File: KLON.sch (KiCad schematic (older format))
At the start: 69 parts, among them IC1 MAX1044ESA+, J1 Conn_01x03, J2 Conn_01x03, J3 Conn_01x02, SW1 3PDT, U1 TL072, U2 TL072

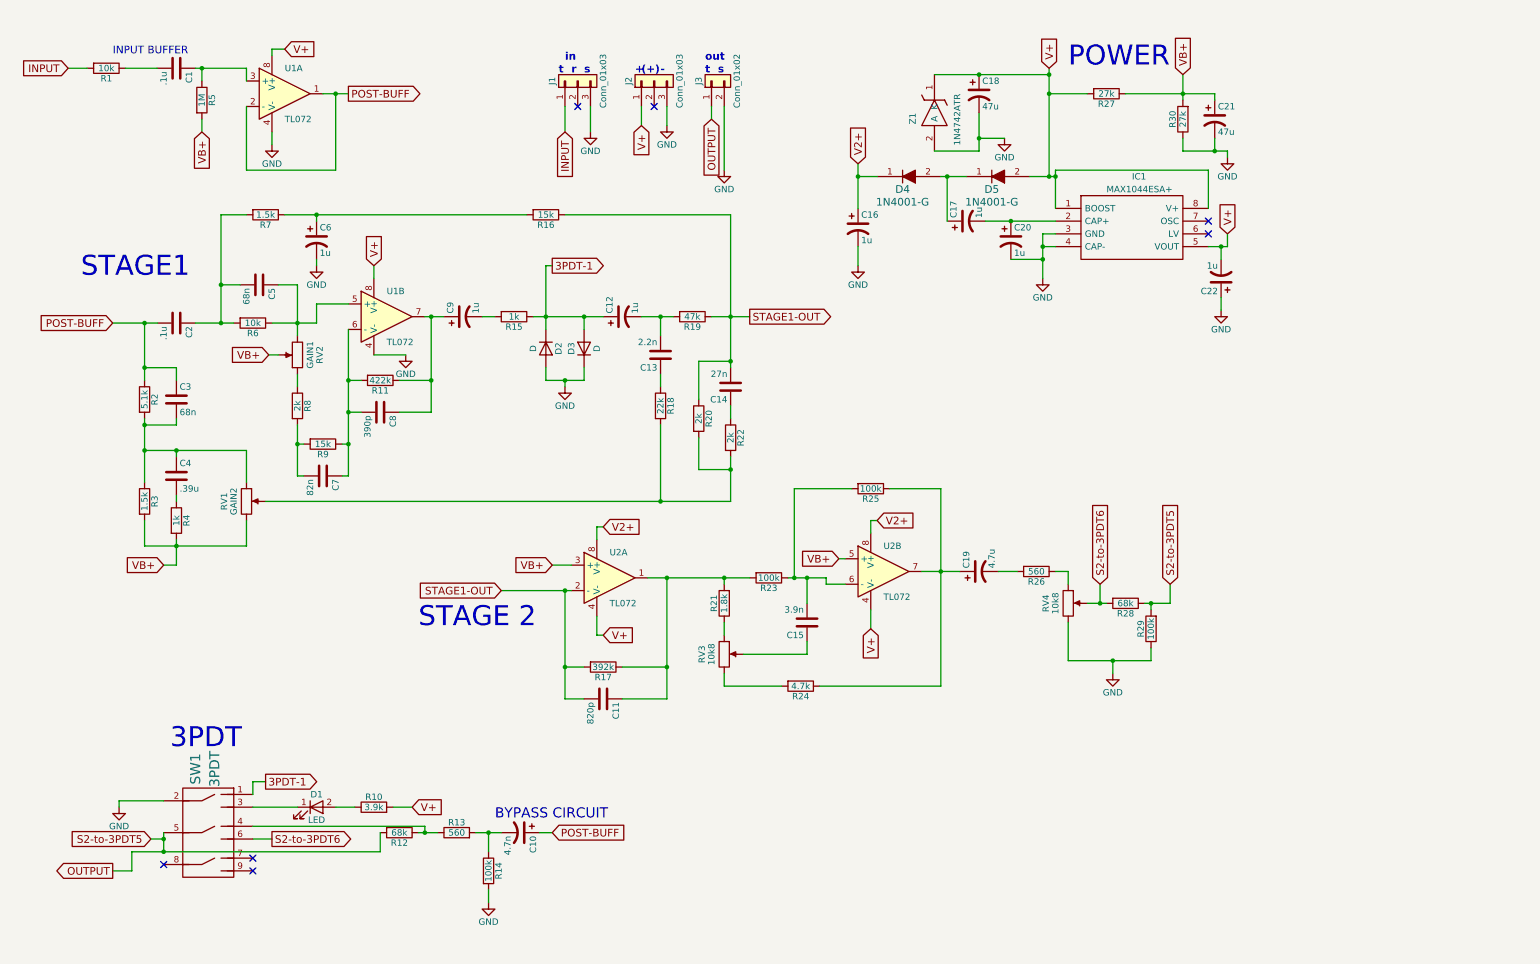
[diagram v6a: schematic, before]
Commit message: added Capacitor Footprints to CSV, added capacitors to digikey BOM (will put link or .xlsx file here later)
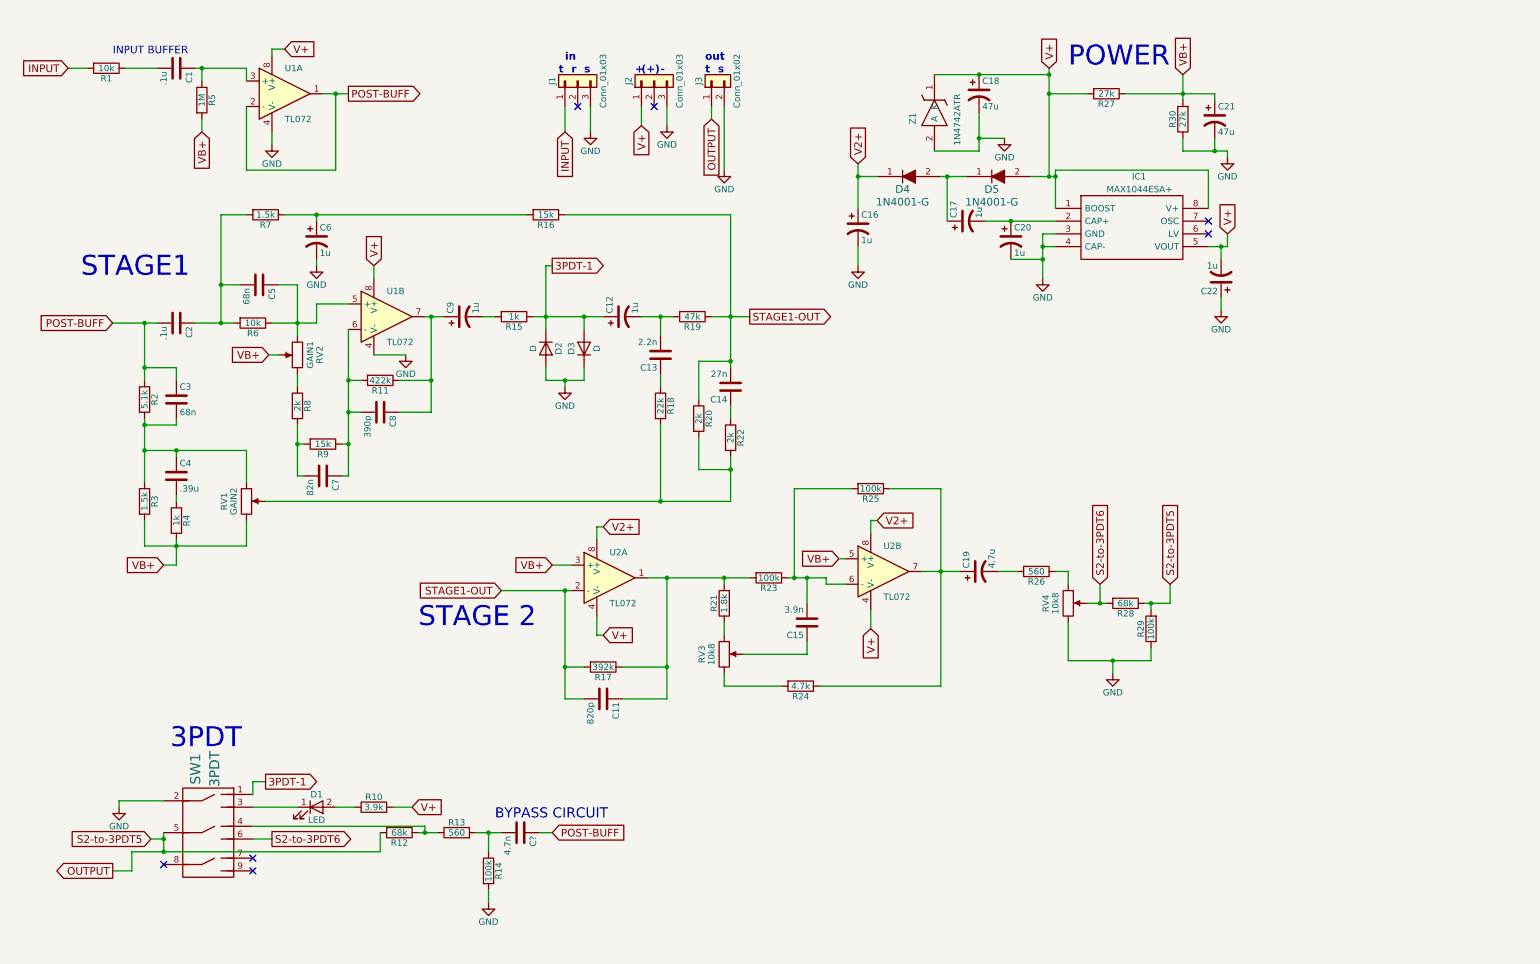
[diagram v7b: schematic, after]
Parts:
- removed C10: 4.7n, Capacitors_THT:C_Rect_L7.0mm_W2.0mm_P5.00mm, symbol CP1
- added C?: 4.7n, symbol C
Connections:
- net POST-BUFF: now also C?.1
- net at R13.2, R14.1: now also C?.2
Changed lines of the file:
@@
 	1300 700  1550 700
 Wire Wire Line
-	1850 700  2250 700
+	1850 700  1900 700
+Wire Wire Line
+	1900 700  2250 700
 Wire Wire Line
 	1900 700  1900 800
@@
 	2950 1500 2950 900
 Wire Wire Line
-	2850 900  3050 900
+	2850 900  2950 900
+Wire Wire Line
+	2950 900  3050 900
 Wire Wire Line
 	2550 550  2450 550
@@
 Connection ~ 2950 900
 Wire Wire Line
-	1850 2700 2150 2700
+	1850 2700 2050 2700
+Wire Wire Line
+	2050 2700 2150 2700
 Wire Wire Line
 	2200 2400 2050 2400
 Wire Wire Line
-	2050 1850 2050 2700
+	2050 1850 2050 2400
+Wire Wire Line
+	2050 2400 2050 2700
 Connection ~ 2050 2700
 Wire Wire Line
-	1200 2700 1550 2700
-Wire Wire Line
-	1450 2700 1450 3150
+	1200 2700 1450 2700
+Wire Wire Line
+	1450 2700 1550 2700
+Wire Wire Line
+	1450 2700 1450 3050
+Wire Wire Line
+	1450 3050 1450 3150
 Connection ~ 1450 2700
 Wire Wire Line
@@
 Connection ~ 2650 2700
 Wire Wire Line
-	2650 2400 2650 2800
+	2650 2400 2650 2700
+Wire Wire Line
+	2650 2700 2650 2800
 Wire Wire Line
 	3050 3900 3000 3900
@@
 	2650 3200 2650 3100
 Wire Wire Line
-	2650 3500 2650 3900
+	2650 3500 2650 3650
+Wire Wire Line
+	2650 3650 2650 3900
 Wire Wire Line
 	2650 3900 2700 3900
@@
 	3450 3150 3700 3150
 Wire Wire Line
-	2450 2700 2800 2700
-Wire Wire Line
-	3050 2750 3050 3900
+	2450 2700 2650 2700
+Wire Wire Line
+	2650 2700 2800 2700
+Wire Wire Line
+	3050 2750 3050 3150
+Wire Wire Line
+	3050 3150 3050 3400
+Wire Wire Line
+	3050 3400 3050 3650
+Wire Wire Line
+	3050 3650 3050 3900
 Wire Wire Line
 	2800 2700 2800 2550
@@
 	3500 2950 3250 2950
 Wire Wire Line
-	2550 1850 4450 1850
+	2550 1850 2800 1850
+Wire Wire Line
+	2800 1850 4450 1850
 Wire Wire Line
 	2800 1850 2800 1900
@@
 Connection ~ 2050 2400
 Wire Wire Line
-	3650 2650 3800 2650
-Wire Wire Line
-	3700 2650 3700 3400
+	3650 2650 3700 2650
+Wire Wire Line
+	3700 2650 3800 2650
+Wire Wire Line
+	3700 2650 3700 3150
+Wire Wire Line
+	3700 3150 3700 3400
 Connection ~ 3700 2650
 Connection ~ 3700 3150
@@
 	4600 3050 4600 3150
 Wire Wire Line
-	4600 3150 4900 3150
+	4600 3150 4750 3150
+Wire Wire Line
+	4750 3150 4900 3150
 Wire Wire Line
 	4900 3150 4900 3050
@@
 	3100 6500 2950 6500
 Wire Wire Line
-	4600 2250 4600 2750
+	4600 2250 4600 2650
+Wire Wire Line
+	4600 2650 4600 2750
 Connection ~ 4600 2650
 Wire Wire Line
@@
 Connection ~ 4900 2650
 Wire Wire Line
-	5350 2650 5600 2650
+	5350 2650 5500 2650
+Wire Wire Line
+	5500 2650 5600 2650
 Wire Wire Line
 	5500 3100 5500 3200
@@
 	1450 4250 1450 4450
 Wire Wire Line
-	1450 4450 2250 4450
+	1450 4450 1700 4450
+Wire Wire Line
+	1700 4450 2250 4450
 Wire Wire Line
 	2250 4450 2250 4250
 Connection ~ 1700 4450
 Wire Wire Line
-	1450 3700 2250 3700
+	1450 3700 1700 3700
+Wire Wire Line
+	1700 3700 2250 3700
 Connection ~ 1450 3700
 Wire Wire Line
@@
 	1700 4050 1700 4100
 Wire Wire Line
-	1700 4400 1700 4600
+	1700 4400 1700 4450
+Wire Wire Line
+	1700 4450 1700 4600
 Wire Wire Line
 	1700 4600 1600 4600
@@
 	4750 1850 6050 1850
 Wire Wire Line
-	6050 1850 6050 3050
-Wire Wire Line
-	5900 2650 6200 2650
-Wire Wire Line
-	6050 4100 2400 4100
-Wire Wire Line
-	6050 3750 6050 4100
-Wire Wire Line
-	1450 3450 1450 3950
-Wire Wire Line
-	4500 2650 5050 2650
+	6050 1850 6050 2650
+Wire Wire Line
+	6050 2650 6050 3000
+Wire Wire Line
+	6050 3000 6050 3050
+Wire Wire Line
+	5900 2650 6050 2650
+Wire Wire Line
+	6050 2650 6200 2650
+Wire Wire Line
+	6050 4100 5500 4100
+Wire Wire Line
+	5500 4100 2400 4100
+Wire Wire Line
+	6050 3750 6050 3850
+Wire Wire Line
+	6050 3850 6050 4100
+Wire Wire Line
+	1450 3450 1450 3500
+Wire Wire Line
+	1450 3500 1450 3700
+Wire Wire Line
+	1450 3700 1450 3950
+Wire Wire Line
+	4500 2650 4600 2650
+Wire Wire Line
+	4600 2650 4900 2650
+Wire Wire Line
+	4900 2650 5050 2650
 Wire Wire Line
 	5500 3500 5500 4100
@@
 Connection ~ 1450 3500
 Wire Wire Line
-	4250 4800 4800 4800
+	4250 4800 4750 4800
+Wire Wire Line
+	4750 4800 4800 4800
 Wire Wire Line
 	5050 4300 5000 4300
@@
 	4650 4600 4800 4600
 Wire Wire Line
-	4750 4800 4750 5650
+	4750 4800 4750 5400
+Wire Wire Line
+	4750 5400 4750 5650
 Wire Wire Line
 	4750 5400 4900 5400
@@
 Connection ~ 4750 5400
 Wire Wire Line
-	5400 4700 6200 4700
-Wire Wire Line
-	5550 4700 5550 5650
+	5400 4700 5550 4700
+Wire Wire Line
+	5550 4700 6000 4700
+Wire Wire Line
+	6000 4700 6200 4700
+Wire Wire Line
+	5550 4700 5550 5400
+Wire Wire Line
+	5550 5400 5550 5650
 Wire Wire Line
 	5550 5400 5200 5400
@@
 	6650 5300 6150 5300
 Wire Wire Line
-	6500 4700 6800 4700
+	6500 4700 6550 4700
+Wire Wire Line
+	6550 4700 6650 4700
+Wire Wire Line
+	6650 4700 6800 4700
 Wire Wire Line
 	6650 4700 6650 4900
 Wire Wire Line
-	7550 4650 7850 4650
-Wire Wire Line
-	7700 4000 7700 5550
+	7550 4650 7700 4650
+Wire Wire Line
+	7700 4650 7850 4650
+Wire Wire Line
+	7700 4000 7700 4650
+Wire Wire Line
+	7700 4650 7700 5550
 Wire Wire Line
 	7700 5550 6750 5550
@@
 	8700 5050 8700 5350
 Wire Wire Line
-	8700 5350 9350 5350
+	8700 5350 9050 5350
+Wire Wire Line
+	9050 5350 9350 5350
 Wire Wire Line
 	9350 5350 9350 5250
@@
 S2-to-3PDT5
 Wire Wire Line
-	9300 4900 9500 4900
+	9300 4900 9350 4900
+Wire Wire Line
+	9350 4900 9500 4900
 Wire Wire Line
 	9500 4900 9500 4750
 Connection ~ 9350 4900
 Wire Wire Line
-	8850 4900 9000 4900
+	8850 4900 8950 4900
+Wire Wire Line
+	8950 4900 9000 4900
 Wire Wire Line
 	9350 4950 9350 4900
@@
 	1500 6750 1600 6750
 Wire Wire Line
-	1600 6700 1600 6850
+	1600 6700 1600 6750
+Wire Wire Line
+	1600 6750 1600 6850
 Text GLabel 4650 6700 2    60   Input ~ 0
 POST-BUFF
-$Comp
-L CP1 C10
-U 1 1 5AB70457
-P 4400 6700
-F 0 "C10" H 4425 6800 50  0000 L CNN
-F 1 "4.7n" H 4425 6600 50  0000 L CNN
-F 2 "Capacitors_THT:C_Rect_L7.0mm_W2.0mm_P5.00mm" H 4400 6700 50  0001 C CNN
-F 3 "" H 4400 6700 50  0001 C CNN
-	1    4400 6700
-	0    1    1    0
-$EndComp
 $Comp
 L R R14
@@
 	4150 6850 4150 6700
 Wire Wire Line
-	4050 6700 4250 6700
+	4050 6700 4150 6700
+Wire Wire Line
+	4150 6700 4250 6700
 Connection ~ 4150 6700
 Wire Wire Line
@@
 $EndComp
 Wire Wire Line
-	3750 6700 3600 6700
+	3750 6700 3650 6700
+Wire Wire Line
+	3650 6700 3600 6700
 Wire Wire Line
 	3650 6700 3650 6650
@@
 	3300 6850 3300 6700
 Wire Wire Line
-	1350 6850 3300 6850
+	1350 6850 1600 6850
+Wire Wire Line
+	1600 6850 3300 6850
 Connection ~ 1600 6750
 Text Notes 4200 6600 0    79   ~ 0
@@
 	9900 2600 9900 2500
 Wire Wire Line
-	9800 2100 9950 2100
+	9800 2100 9900 2100
+Wire Wire Line
+	9900 2100 9950 2100
 Wire Wire Line
 	9900 2100 9900 2200
@@
 	8600 2000 8500 2000
 Wire Wire Line
-	8500 2000 8500 2350
+	8500 2000 8500 2100
+Wire Wire Line
+	8500 2100 8500 2200
+Wire Wire Line
+	8500 2200 8500 2350
 Wire Wire Line
 	8600 2100 8500 2100
@@
 Connection ~ 8500 2200
 Wire Wire Line
-	8050 1900 8600 1900
+	8050 1900 8250 1900
+Wire Wire Line
+	8250 1900 8600 1900
 $Comp
 L CP1 C17
@@
 	7750 1900 7750 1550
 Wire Wire Line
-	7700 1550 7900 1550
+	7700 1550 7750 1550
+Wire Wire Line
+	7750 1550 7900 1550
 Connection ~ 7750 1550
 $Comp
@@
 $EndComp
 Wire Wire Line
-	7050 1450 7050 1800
+	7050 1450 7050 1550
+Wire Wire Line
+	7050 1550 7050 1800
 Wire Wire Line
 	7050 1550 7200 1550
@@
 	9800 1500 8600 1500
 Wire Wire Line
-	8600 1500 8600 1800
-Wire Wire Line
-	8400 1550 8600 1550
+	8600 1500 8600 1550
+Wire Wire Line
+	8600 1550 8600 1800
+Wire Wire Line
+	8400 1550 8550 1550
+Wire Wire Line
+	8550 1550 8600 1550
 Connection ~ 8600 1550
 Text GLabel 8550 700  1    60   Input ~ 0
@@
 Connection ~ 8550 1550
 Wire Wire Line
-	8550 700  8550 1550
+	8550 700  8550 750
+Wire Wire Line
+	8550 750  8550 900
+Wire Wire Line
+	8550 900  8550 1550
 $Comp
 L R R27
@@
 $EndComp
 Wire Wire Line
-	7650 750  8550 750
+	7650 750  8000 750
+Wire Wire Line
+	8000 750  8550 750
 Connection ~ 8550 750
 Connection ~ 8000 750
@@
 $EndComp
 Wire Wire Line
-	8000 1050 8000 1350
+	8000 1050 8000 1250
+Wire Wire Line
+	8000 1250 8000 1350
 Wire Wire Line
 	8000 1350 7650 1350
@@
 VB+
 Wire Wire Line
-	9150 900  9850 900
-Wire Wire Line
-	9600 750  9600 950
+	9150 900  9600 900
+Wire Wire Line
+	9600 900  9850 900
+Wire Wire Line
+	9600 750  9600 900
+Wire Wire Line
+	9600 900  9600 950
 $Comp
 L R R30
@@
 	9600 1250 9600 1350
 Wire Wire Line
-	9600 1350 9950 1350
+	9600 1350 9850 1350
+Wire Wire Line
+	9850 1350 9950 1350
 Wire Wire Line
 	9950 1350 9950 1400
@@
 Wire Wire Line
 	6000 1500 6000 1000
+$Comp
+L C C?
+U 1 1 5AE93261
+P 4400 6700
+F 0 "C?" H 4425 6800 50  0000 L CNN
+F 1 "4.7n" H 4425 6600 50  0000 L CNN
+F 2 "" H 4438 6550 50  0001 C CNN
+F 3 "" H 4400 6700 50  0001 C CNN
+	1    4400 6700
+	0    1    1    0
+$EndComp
 $EndSCHEMATC
